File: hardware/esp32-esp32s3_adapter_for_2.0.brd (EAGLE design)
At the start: 21.5 x 26.4 mm, 3 parts, among them U1 ESP32-S3-WROOM-1-N16R2, U2 ESP32-WROOM-32E_(16MB)

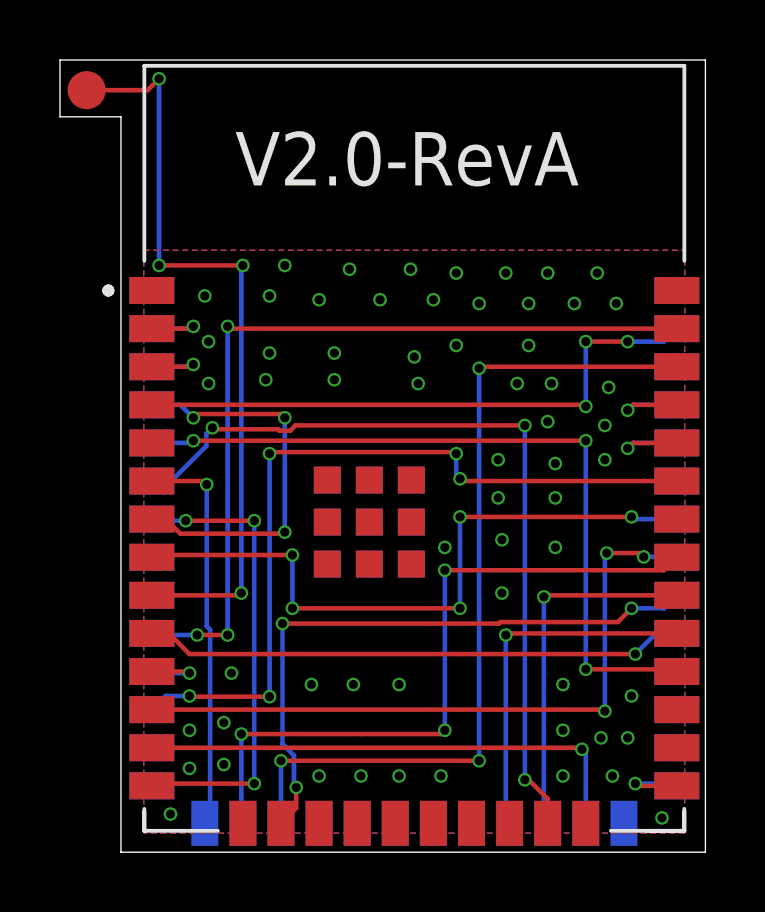
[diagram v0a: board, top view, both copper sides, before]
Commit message: Added RevB of ESP32toESP32S3 V1.4 and 2.0
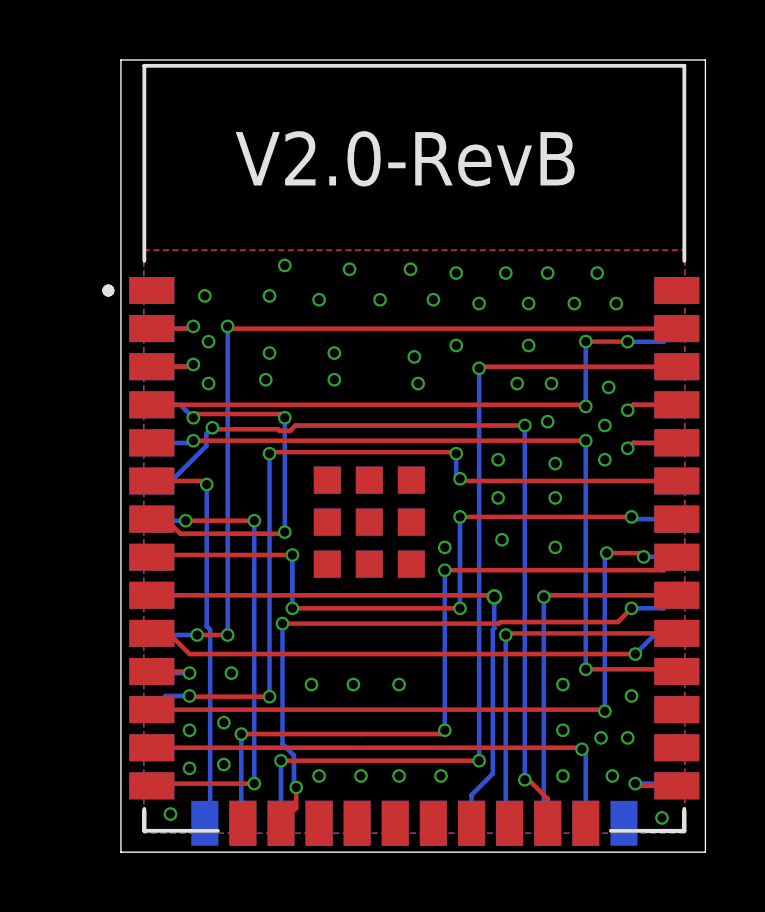
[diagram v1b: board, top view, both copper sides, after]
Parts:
- removed TP1: TPB1,27, testpad:B1,27
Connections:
- removed net FREE_SPI_CS1: U1.22
- net SQL: now also U1.22; no longer TP1.TP
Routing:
- net SQL: track 25.5 -> 19.3 mm, vias 4 -> 1
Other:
- board size 21.5 x 26.4 mm -> 19.5 x 26.4 mm
- board text added: "V2.0-RevB"
- board text removed: "V2.0-RevA"
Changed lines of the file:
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@@
 <wire x1="3.683" y1="53.34" x2="23.165" y2="53.34" width="0" layer="20"/>
 <wire x1="23.165" y1="53.34" x2="23.165" y2="79.746" width="0" layer="20"/>
-<wire x1="23.165" y1="79.746" x2="1.651" y2="79.746" width="0" layer="20"/>
-<wire x1="1.651" y1="79.746" x2="1.651" y2="77.851" width="0" layer="20"/>
-<wire x1="1.651" y1="77.851" x2="3.683" y2="77.851" width="0" layer="20"/>
-<wire x1="3.683" y1="77.851" x2="3.683" y2="53.34" width="0" layer="20"/>
-<text x="7.493" y="75.565" size="1.778" layer="25">V2.0-RevA</text>
+<wire x1="23.165" y1="79.746" x2="3.683" y2="79.746" width="0" layer="20"/>
+<wire x1="3.683" y1="79.746" x2="3.683" y2="53.34" width="0" layer="20"/>
+<text x="7.493" y="75.565" size="1.778" layer="25">V2.0-RevB</text>
 </plain>
 <attributes>
@@
 <attribute name="PRICE" value="None" x="41.402" y="18.542" size="1.778" layer="27" display="off"/>
 </element>
-<element name="TP1" library="testpad" library_urn="urn:adsk.eagle:library:385" package="B1,27" package3d_urn="urn:adsk.eagle:package:27944/2" value="TPB1,27" x="2.54" y="78.74" smashed="yes">
-<attribute name="POPULARITY" value="19" x="2.54" y="78.74" size="1.778" layer="27" display="off"/>
-<attribute name="TP_SIGNAL_NAME" value="" x="2.54" y="78.74" size="1.778" layer="27" display="off"/>
-<attribute name="VALUE" x="1.905" y="77.978" size="0.0254" layer="27"/>
-</element>
 </elements>
 <signals>
@@
 <via x="16.256" y="65.151" extent="1-16" drill="0.3048"/>
 <via x="16.383" y="63.754" extent="1-16" drill="0.3048"/>
-<via x="16.383" y="61.976" extent="1-16" drill="0.3048"/>
 <via x="19.812" y="66.421" extent="1-16" drill="0.3048"/>
 <via x="19.812" y="67.564" extent="1-16" drill="0.3048"/>
@@
 <signal name="SQL">
 <contactref element="U2" pad="9"/>
-<contactref element="TP1" pad="TP"/>
-<wire x1="4.712" y1="61.902" x2="7.546" y2="61.902" width="0.1524" layer="1"/>
-<wire x1="7.546" y1="61.902" x2="7.62" y2="61.976" width="0.1524" layer="1"/>
-<wire x1="7.62" y1="61.976" x2="7.6962" y2="61.976" width="0.1524" layer="1"/>
-<via x="7.6962" y="61.976" extent="1-16" drill="0.3048"/>
-<wire x1="7.6962" y1="61.976" x2="7.6962" y2="72.8472" width="0.1524" layer="16"/>
-<wire x1="7.6962" y1="72.8472" x2="7.747" y2="72.898" width="0.1524" layer="16"/>
-<via x="7.747" y="72.898" extent="1-16" drill="0.3048"/>
-<wire x1="7.747" y1="72.898" x2="4.953" y2="72.898" width="0.1524" layer="1"/>
-<via x="4.953" y="72.898" extent="1-16" drill="0.3048"/>
-<wire x1="4.953" y1="72.898" x2="4.953" y2="79.121" width="0.1524" layer="16"/>
-<via x="4.953" y="79.121" extent="1-16" drill="0.3048"/>
-<wire x1="4.953" y1="79.121" x2="4.572" y2="78.74" width="0.1524" layer="1"/>
-<wire x1="4.572" y1="78.74" x2="2.54" y2="78.74" width="0.1524" layer="1"/>
-</signal>
-<signal name="FREE_SPI_CS1">
 <contactref element="U1" pad="22"/>
+<wire x1="4.712" y1="61.902" x2="16.076" y2="61.902" width="0.1524" layer="1"/>
+<wire x1="16.076" y1="61.902" x2="16.129" y2="61.849" width="0.1524" layer="1"/>
+<via x="16.129" y="61.849" extent="1-16" drill="0.35"/>
+<wire x1="16.129" y1="61.849" x2="16.129" y2="60.8086625" width="0.1524" layer="16"/>
+<wire x1="16.129" y1="60.8086625" x2="16.0782" y2="60.7578625" width="0.1524" layer="16"/>
+<wire x1="16.0782" y1="55.9562" x2="15.367" y2="55.245" width="0.1524" layer="16"/>
+<wire x1="16.0782" y1="60.7578625" x2="16.0782" y2="55.9562" width="0.1524" layer="16"/>
+<wire x1="15.367" y1="55.245" x2="15.367" y2="54.302" width="0.1524" layer="16"/>
 </signal>
 <signal name="MIC_CH_SEL">
@@
 </board>
 </drawing>
-<compatibility>
-<note version="8.2" severity="warning">
-Since Version 8.2, EAGLE supports online libraries. The ids
-of those online libraries will not be understood (or retained)
-with this version.
-</note>
-<note version="8.3" severity="warning">
-Since Version 8.3, EAGLE supports URNs for individual library
-assets (packages, symbols, and devices). The URNs of those assets
-will not be understood (or retained) with this version.
-</note>
-<note version="8.3" severity="warning">
-Since Version 8.3, EAGLE supports the association of 3D packages
-with devices in libraries, schematics, and board files. Those 3D
-packages will not be understood (or retained) with this version.
-</note>
-</compatibility>
 </eagle>

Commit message: - T-TWR PLUS V2.0 MOD board support added
- ESP32S3 -> ESP32E adapter Rev.C added
- AudioAdapter BOM fix (4k7->33k)
- README.md updated
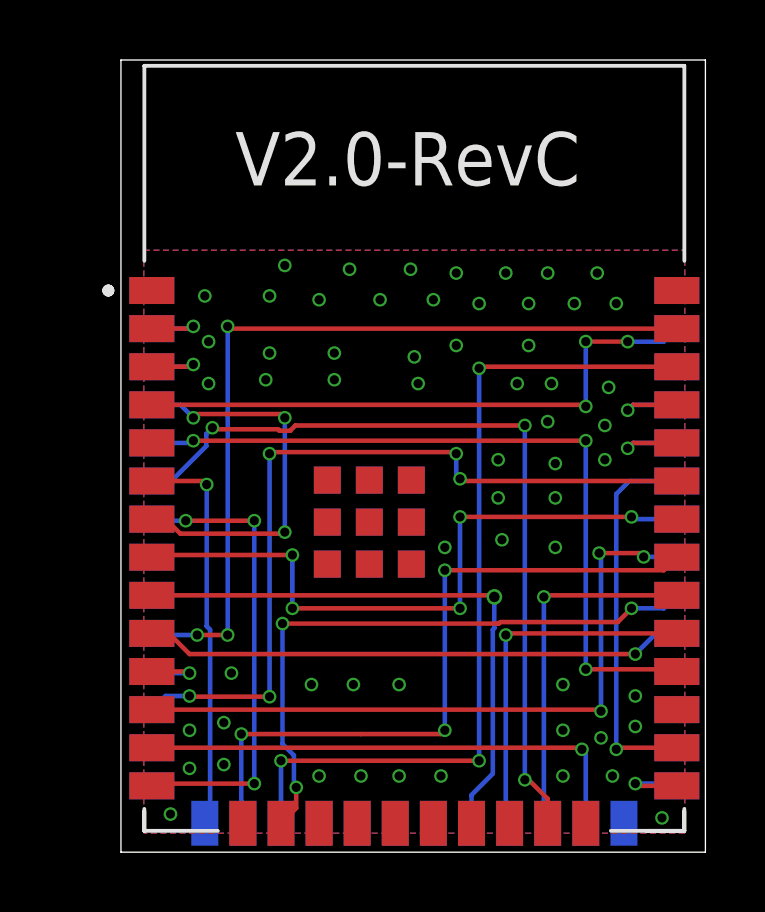
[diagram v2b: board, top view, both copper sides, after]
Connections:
- removed net TXLED(NC): U2.26
- net PIXES: now also U2.26
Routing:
- net PIXES: track 0.00 -> 12.7 mm, vias 0 -> 1
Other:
- board text added: "V2.0-RevC"
- board text removed: "V2.0-RevB"
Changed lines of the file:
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@@
 <wire x1="23.165" y1="79.746" x2="3.683" y2="79.746" width="0" layer="20"/>
 <wire x1="3.683" y1="79.746" x2="3.683" y2="53.34" width="0" layer="20"/>
-<text x="7.493" y="75.565" size="1.778" layer="25">V2.0-RevB</text>
+<text x="7.493" y="75.565" size="1.778" layer="25">V2.0-RevC</text>
 </plain>
 <attributes>
@@
 <via x="12.954" y="55.88" extent="1-16" drill="0.3048"/>
 <via x="14.351" y="55.88" extent="1-16" drill="0.3048"/>
-<via x="20.574" y="57.15" extent="1-16" drill="0.3048"/>
+<via x="20.828" y="57.531" extent="1-16" drill="0.3048"/>
 <via x="20.066" y="55.88" extent="1-16" drill="0.3048"/>
 <via x="19.685" y="57.15" extent="1-16" drill="0.3048"/>
@@
 <via x="18.415" y="57.404" extent="1-16" drill="0.3048"/>
 <via x="18.415" y="55.88" extent="1-16" drill="0.3048"/>
-<via x="20.701" y="58.547" extent="1-16" drill="0.3048"/>
+<via x="20.828" y="58.547" extent="1-16" drill="0.3048"/>
 <via x="18.161" y="63.5" extent="1-16" drill="0.3048"/>
 <via x="18.161" y="65.151" extent="1-16" drill="0.3048"/>
@@
 <contactref element="U2" pad="12"/>
 <wire x1="22.138" y1="63.246" x2="22.212" y2="63.172" width="0.1524" layer="16"/>
-<wire x1="4.712" y1="58.092" x2="19.759" y2="58.092" width="0.1524" layer="1"/>
-<wire x1="19.759" y1="58.092" x2="19.812" y2="58.039" width="0.1524" layer="1"/>
-<via x="19.812" y="58.039" extent="1-16" drill="0.3048"/>
-<wire x1="19.812" y1="58.039" x2="19.812" y2="63.119" width="0.1524" layer="16"/>
-<wire x1="19.812" y1="63.119" x2="19.939" y2="63.246" width="0.1524" layer="16"/>
-<wire x1="19.939" y1="63.246" x2="19.8755" y2="63.3095" width="0.1524" layer="16"/>
-<via x="19.8755" y="63.3095" extent="1-16" drill="0.3048"/>
-<wire x1="19.8755" y1="63.3095" x2="21.1455" y2="63.3095" width="0.1524" layer="1"/>
+<wire x1="4.712" y1="58.092" x2="19.632" y2="58.092" width="0.1524" layer="1"/>
+<wire x1="19.632" y1="58.092" x2="19.685" y2="58.039" width="0.1524" layer="1"/>
+<via x="19.685" y="58.039" extent="1-16" drill="0.3048"/>
+<wire x1="19.6215" y1="63.3095" x2="19.685" y2="63.246" width="0.1524" layer="16"/>
+<wire x1="19.685" y1="63.246" x2="19.685" y2="58.039" width="0.1524" layer="16"/>
+<via x="19.6215" y="63.3095" extent="1-16" drill="0.3048"/>
+<wire x1="19.6215" y1="63.3095" x2="21.1455" y2="63.3095" width="0.1524" layer="1"/>
 <wire x1="21.1455" y1="63.3095" x2="21.209" y2="63.246" width="0.1524" layer="1"/>
 <wire x1="21.209" y1="63.246" x2="21.1455" y2="63.1825" width="0.1524" layer="1"/>
@@
 <signal name="N$42">
 <contactref element="U2" pad="5"/>
-</signal>
-<signal name="TXLED(NC)">
-<contactref element="U2" pad="26"/>
 </signal>
 <signal name="GPS_RXD">
@@
 <signal name="PIXES">
 <contactref element="U1" pad="35"/>
+<contactref element="U2" pad="26"/>
+<wire x1="22.212" y1="65.712" x2="20.627" y2="65.712" width="0.1524" layer="16"/>
+<wire x1="20.627" y1="65.712" x2="20.193" y2="65.278" width="0.1524" layer="16"/>
+<via x="20.193" y="56.769" extent="1-16" drill="0.3048"/>
+<wire x1="20.193" y1="56.769" x2="20.246" y2="56.822" width="0.1524" layer="1"/>
+<wire x1="20.246" y1="56.822" x2="22.212" y2="56.822" width="0.1524" layer="1"/>
+<wire x1="20.193" y1="65.278" x2="20.193" y2="56.769" width="0.1524" layer="16"/>
 </signal>
 <signal name="FREE_RX1">
